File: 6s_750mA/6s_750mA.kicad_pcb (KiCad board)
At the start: 2 copper layers, 71.8 x 55.9 mm, 93 parts, among them J1 Barrel_Jack_MountingPin, J2 S6B-XH-A, U1 SN6505BDBV, U10 BQ25170DSGR, U11 SN6505BDBV, U12 BQ25170DSGR, U2 BQ25170DSGR, U3 SN6505BDBV, U4 BQ25170DSGR, U5 SN6505BDBV, U6 BQ25170DSGR, U7 SN6505BDBV, U8 BQ25170DSGR, U9 SN6505BDBV

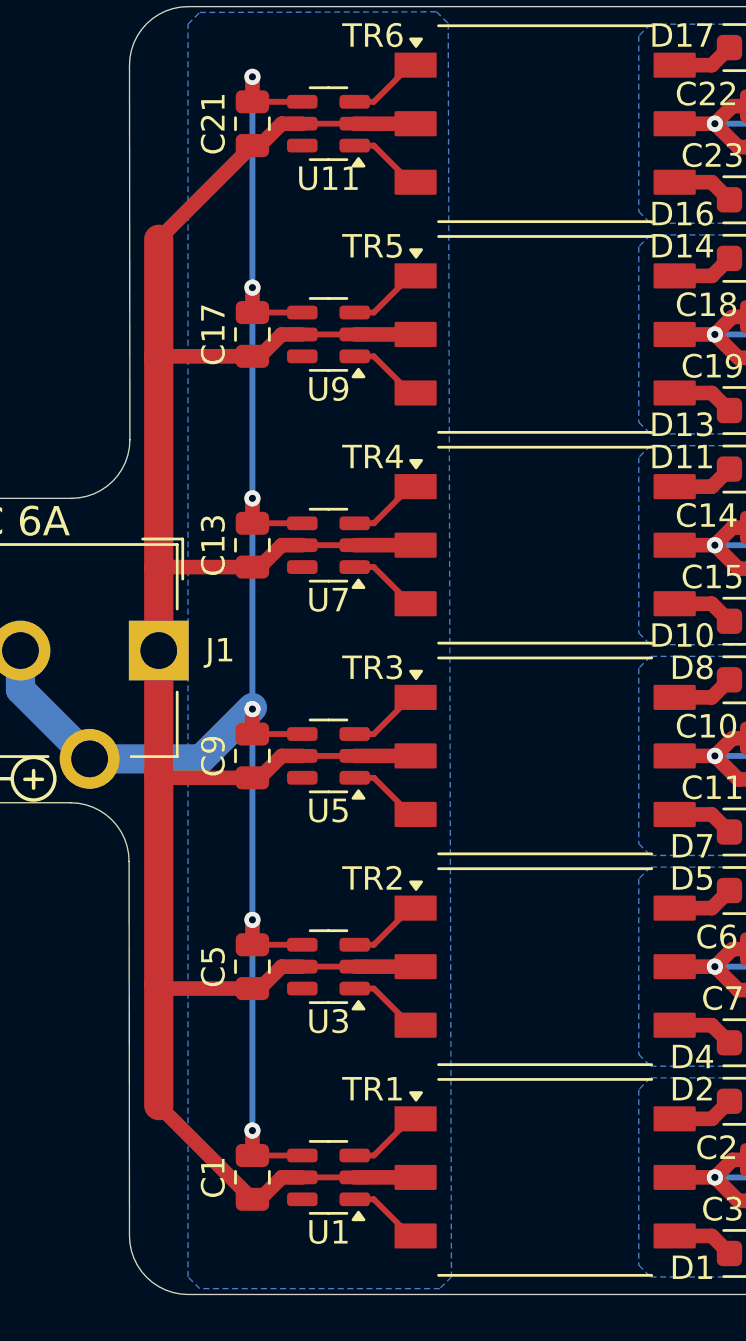
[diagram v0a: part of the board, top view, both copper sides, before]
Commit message: add logos and CC icons to bottom
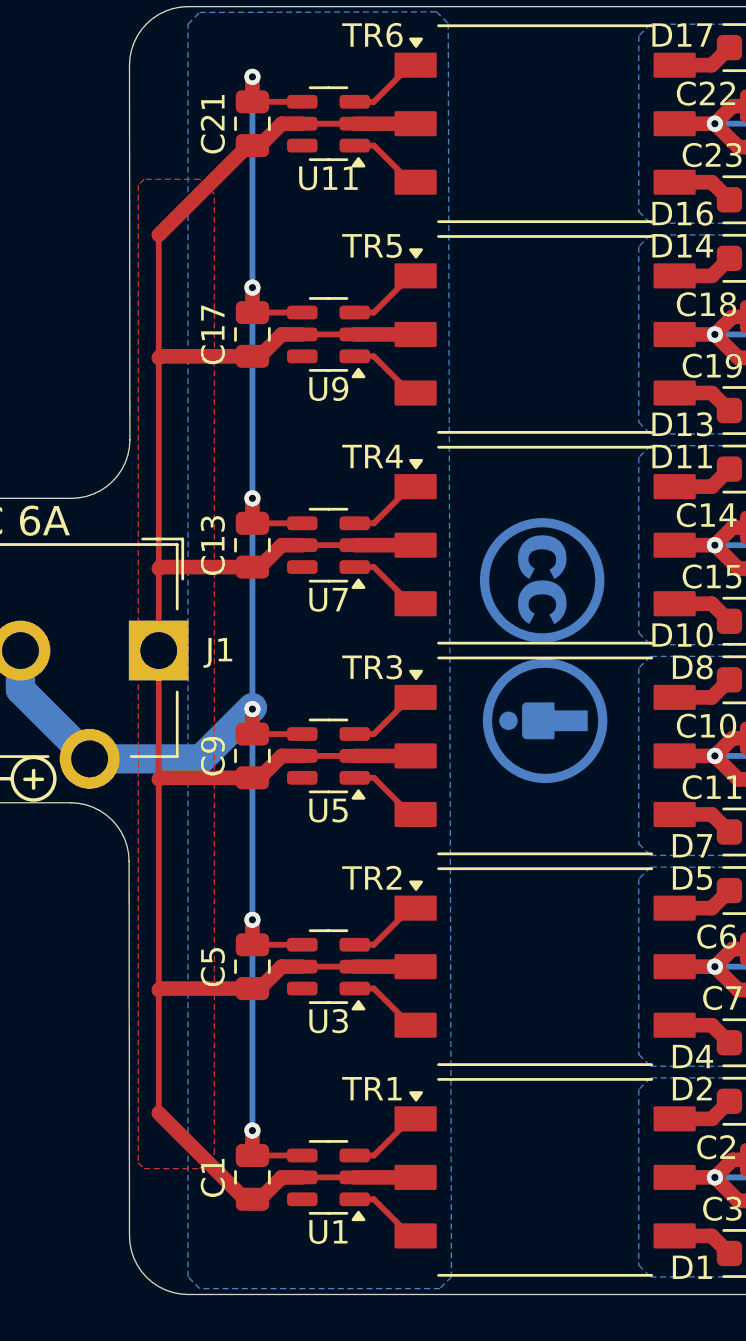
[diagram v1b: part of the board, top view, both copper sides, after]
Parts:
- added REF**: KiCad-Logo2_5mm_SilkScreen, Symbol:KiCad-Logo2_5mm_SilkScreen, B.Cu at (202.1, 87.4)
- added REF**: Symbol_CC-Attribution_CopperTop_Small, Symbol:Symbol_CC-Attribution_CopperTop_Small, B.Cu at (164.3, 90.4)
- added REF**: Symbol_CreativeCommons_CopperTop_Type2_Small, Symbol:Symbol_CreativeCommons_CopperTop_Type2_Small, B.Cu at (164.2, 84.3)
- added REF**: OSHW-Logo2_7.3x6mm_SilkScreen, Symbol:OSHW-Logo2_7.3x6mm_SilkScreen, B.Cu at (190.6, 87.4)
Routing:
- added copper zone on F.Cu, net +5V
